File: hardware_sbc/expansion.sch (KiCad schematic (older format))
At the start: 3 parts, among them J11 DF40HC(3.5)-60DS, J12 DF40HC(3.5)-60DS, U1 IMX8MM

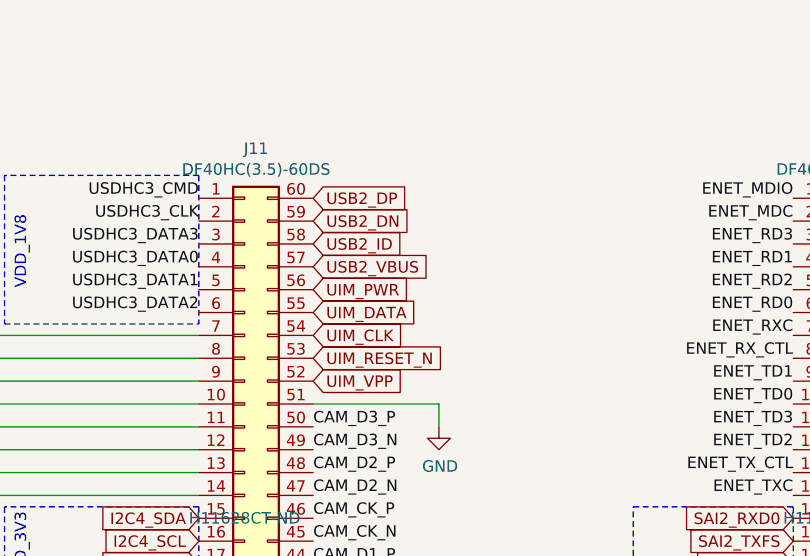
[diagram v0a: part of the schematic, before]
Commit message: Add vbus to expansion connector and bugfix for battery cutoff
This will allow lids to supply power to charge the battery.

The battery cutoff circuit needs V- connected to pack ground, so
this was also fixed.
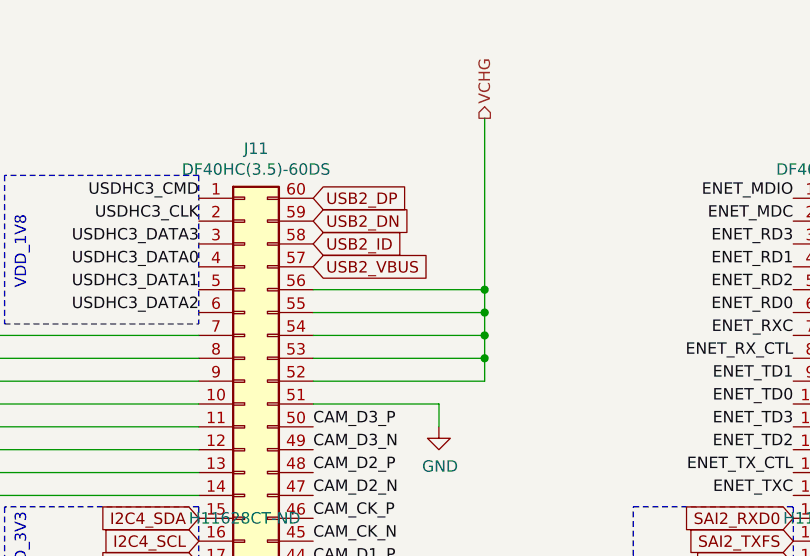
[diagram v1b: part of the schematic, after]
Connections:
- net UIM_DATA is gone; now on net VCHG: J11.55 (Pin_55)
- net UIM_PWR is gone; now on net VCHG: J11.56 (Pin_56)
- net UIM_RESET_N is gone; now on net VCHG: J11.53 (Pin_53)
- net UIM_VPP is gone; now on net VCHG: J11.52 (Pin_52)
- net UIM_CLK renamed VCHG
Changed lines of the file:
@@
 Text GLabel 6000 2900 0    50   Input ~ 0
 I2C4_SCL
-Text GLabel 6500 2100 2    50   Input ~ 0
-UIM_RESET_N
-Text GLabel 6500 2000 2    50   Input ~ 0
-UIM_CLK
-Text GLabel 6500 1900 2    50   Input ~ 0
-UIM_DATA
-Text GLabel 6500 1800 2    50   Input ~ 0
-UIM_PWR
-Text GLabel 6500 2200 2    50   Input ~ 0
-UIM_VPP
 $Comp
 L power:GND #PWR0187
@@
 Wire Wire Line
 	9950 1600 9950 1700
+Text HLabel 7250 1050 1    50   Output ~ 0
+VCHG
+Wire Wire Line
+	6500 1800 7250 1800
+Wire Wire Line
+	7250 1800 7250 1050
+Wire Wire Line
+	6500 1900 7250 1900
+Wire Wire Line
+	7250 1900 7250 1800
+Connection ~ 7250 1800
+Wire Wire Line
+	6500 2000 7250 2000
+Wire Wire Line
+	7250 2000 7250 1900
+Connection ~ 7250 1900
+Wire Wire Line
+	6500 2100 7250 2100
+Wire Wire Line
+	7250 2100 7250 2000
+Connection ~ 7250 2000
+Wire Wire Line
+	6500 2200 7250 2200
+Wire Wire Line
+	7250 2200 7250 2100
+Connection ~ 7250 2100
 $EndSCHEMATC
